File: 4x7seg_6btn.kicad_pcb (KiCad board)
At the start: 2 copper layers, 91.8 x 26.3 mm, 94 parts, among them CON1 AVR-ISP, IC1 ATTINY88-A, Q1 2N7002, Q2 2N7002, Q3 2N7002, Q4 2N7002, Q5 2N7002, Q6 2N7002, U1 74HC14D_653, U10 MC14543B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

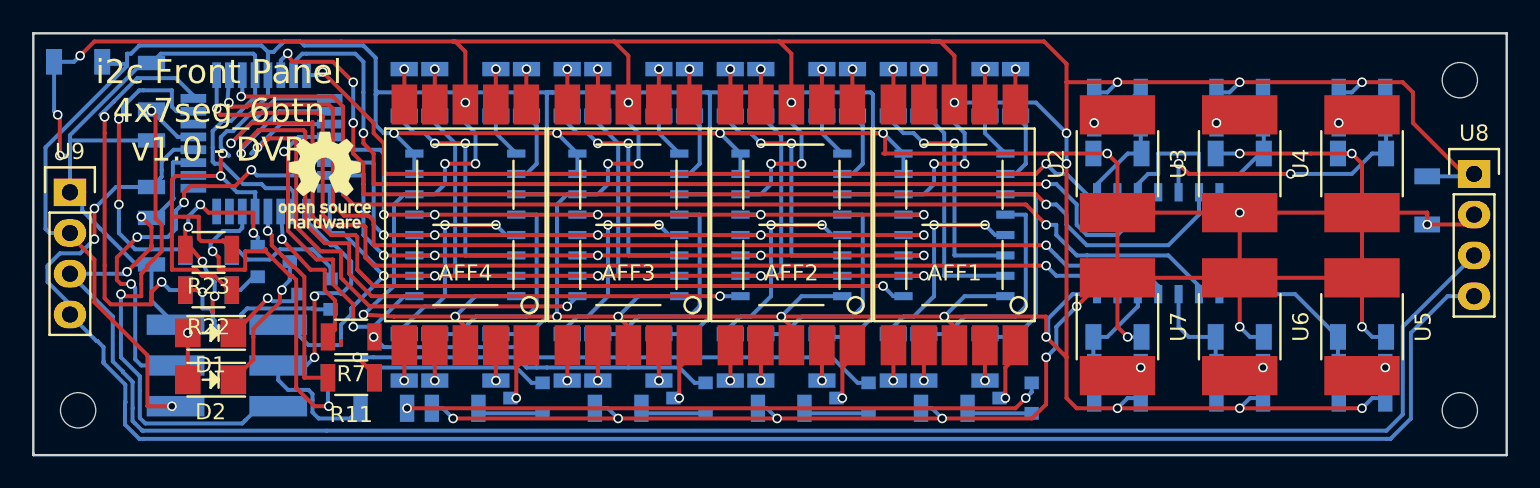
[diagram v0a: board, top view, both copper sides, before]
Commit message: Headers aligned better
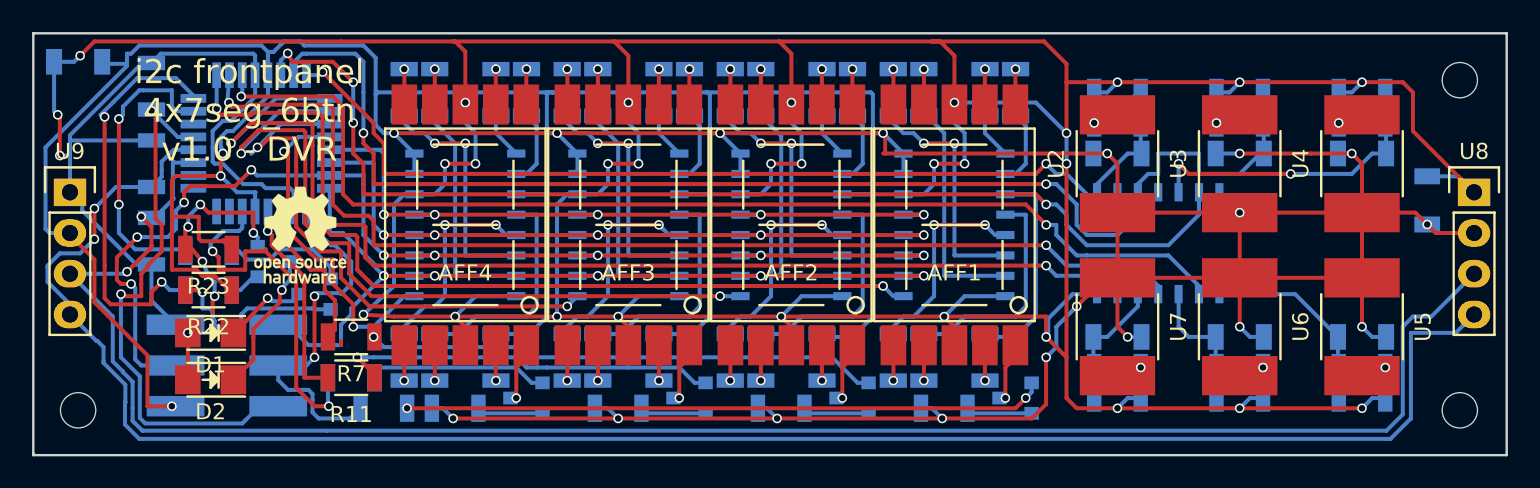
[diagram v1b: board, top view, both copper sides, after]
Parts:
- moved REF*** 3.75 mm to (49.4, 33.7)
- moved U8 1.14 mm to (122.6, 31.0)
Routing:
- net VCC: track 363.6 -> 364.7 mm
- net GND: track 324.5 -> 323.5 mm
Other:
- board text added: "i2c frontpanel 4x7seg_6btn v1.0 - DVR"
- board text removed: "i2c Front Panel 4x7seg_6btn v1.0 - DVR"
